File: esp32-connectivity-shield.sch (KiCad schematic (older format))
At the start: 23 parts, among them J1 DB9, P1 POWER, P2 Analog, P3 Digital, P4 Digital, P5 CONN_01X01, P6 CONN_01X01, P7 CONN_01X01, P8 CONN_01X01, U1 MCP2515-I/ST, U2 MCP2551-I/SN, Y1 16MHz

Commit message: update schematic-ethernet
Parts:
- removed C?: 0.1uF, symbol C
- removed J1: DB9, symbol DB9
- removed U1: MCP2515-I/ST, Housings_SSOP:TSSOP-20_4.4x6.5mm_Pitch0.65mm, symbol MCP2515-I/ST
- removed Y1: 16MHz, symbol Crystal
- added C10, C11, C13, C14, C15, C16, C7: 100nF, symbol C
- added C12, C8: 10u/6v3, symbol C
- added C9: 10uF/6v3, symbol C
- added J?: RJ45_LEDS, symbol RJ45_LEDS
- added L1: Ferrite_Bead CB2012D601ST, symbol Ferrite_Bead
- added L2: Ferrite_Bead, symbol Ferrite_Bead
- added P9: CONN_01X04, symbol CONN_01X04
- added R10, R13, R14, R5, R6, R7, R8, R9: 4K7, symbol R
- added R11: OR, symbol R
- added R12: 10K, symbol R
- added R15: 6k4, symbol R
- added R16, R17, R18: 330R, symbol R
- added R19: 2K2, symbol R
- added R20, R21, R22, R23: 47R, symbol R
- added U1: KS8721BL, symbol KS8721BL
- added Y1: 50MHz Crystal C7050, symbol Crystal_GND24_Small
- C1: value 22pF -> 100nF
- C2: value 22pF -> 10nF
- C3: value 0.1uF -> 100nF
- R1: value 4.7K -> 4K7
- R2: value 4.7k -> 4K7
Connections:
- net labels added: ETHERNET, ETH_RST, GPIO32, GPIO33, HEADER, LAN+2V5, LAN_RX+, LAN_RX-, LAN_TX+, LAN_TX-, LED100/DUP, LEDACT, RMII_CRS_DV, RMII_MDC, RMII_MDINT, RMII_MDIO, RMII_REF_CLK, RMII_RXD0, RMII_RXD1, RMII_TXD0, RMII_TX_EN
- net labels removed: CSO, INTO, MISO, MOSI, SCK
- wire segments 78 -> 266
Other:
- moved on the sheet: C4, C5, R3, R4, U2

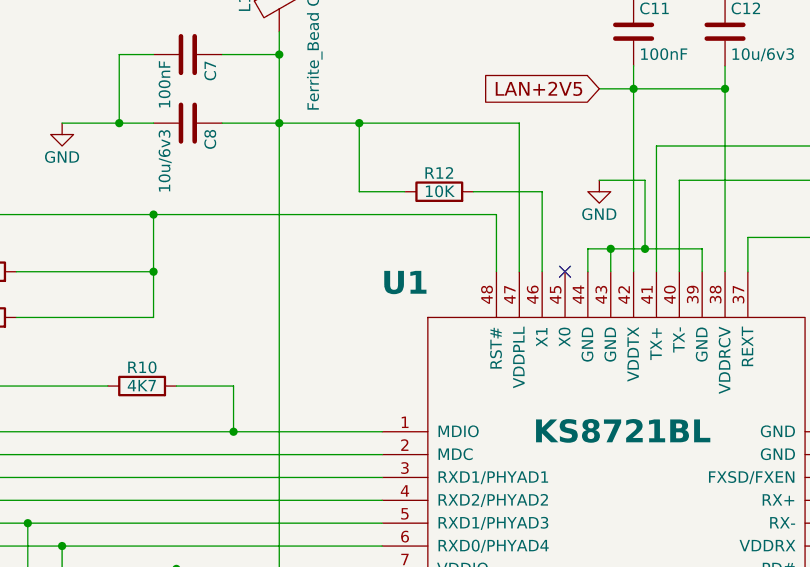
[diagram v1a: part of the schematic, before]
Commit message: fix libray error
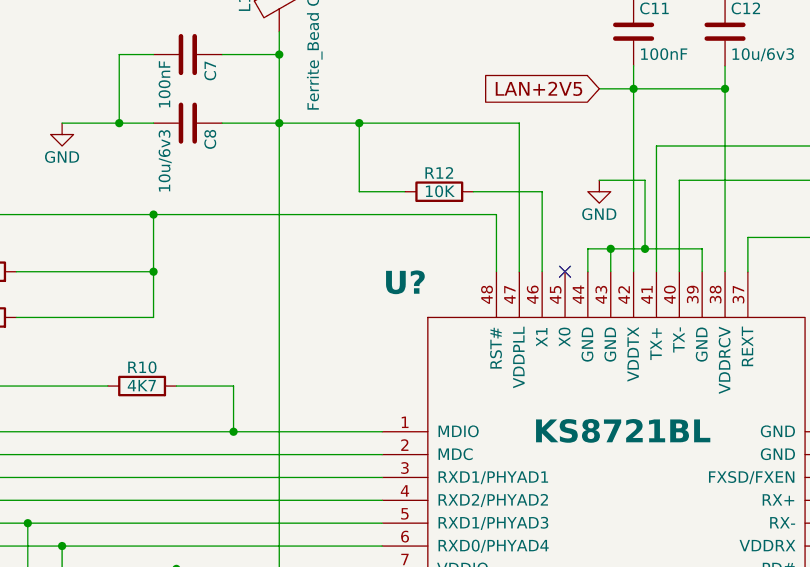
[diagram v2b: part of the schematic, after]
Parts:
- removed U1: KS8721BL, symbol KS8721BL
- added U?: KS8721BL, symbol KS8721BL
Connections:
- net 3V3: now also U?.24 (VDDIO), U?.7 (VDDIO)
- net GND: now also U?.12 (GND), U?.14 (TXER), U?.19 (TXD2), U?.20 (TXD3), U?.23 (GND), U?.35 (GND), U?.36 (GND), U?.39 (GND), U?.43 (GND), U?.44 (GND), U?.8 (GND)
- net LAN+2V5: now also U?.31 (VDDRX), U?.38 (VDDRCV), U?.42 (VDDTX)
- net LAN_RX+: now also U?.33 (RX+)
- net LAN_RX-: now also U?.32 (RX-)
- net LAN_TX+: now also U?.41 (TX+)
- net LAN_TX-: now also U?.40 (TX-)
- net RMII_CRS_DV: now also U?.9 (RXDV/PCS_LPBK)
- net RMII_MDC: now also U?.2 (MDC)
- net RMII_MDIO: now also U?.1 (MDIO)
- net RMII_REF_CLK: now also U?.15 (TXC/REF_CLK)
- net RMII_RXD0: now also U?.6 (RXD0/PHYAD4)
- net RMII_RXD1: now also U?.18 (TXD1), U?.5 (RXD1/PHYAD3)
- net RMII_TXD0: now also U?.17 (TXD0)
- net RMII_TX_EN: now also U?.16 (TXEN)
- net at C10.1, C9.1, L2.1: now also U?.13 (VDDC)
- net at R13.1: now also U?.21 (COL/RMII)
- net at R14.1: now also U?.22 (CRS/RMII_BTB)
- net at R18.2: now also U?.25 (INT#PHYAD0)
- net at R17.2: now also U?.26 (LED0/TEST)
- net at R16.2: now also U?.27 (LED1/SPD100)
- net at R1.1: now also U?.3 (RXD1/PHYAD1)
- net at R15.1: now also U?.37 (REXT)
- net at R6.1: now also U?.4 (RXD2/PHYAD2)
- net at R12.2: now also U?.46 (X1)
- net at C7.1, C8.1, L1.1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: now also U?.47 (VDDPLL)
- net at C1.1, R2.2, R5.2: now also U?.48 (RST#)
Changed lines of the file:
@@
 GPIO33
-$Comp
-L KS8721BL U1
-U 1 1 58756829
-P 5350 5600
-F 0 "U1" H 4300 6800 100 0000 C CNB
-F 1 "KS8721BL" H 5250 6150 100 0000 C CNB
-F 2 "" H 5300 4800 60  0001 C CNN
-F 3 "" H 5300 4800 60  0001 C CNN
-	1    5350 5600
-	1    0    0    -1
-$EndComp
 $Comp
 L R R10
@@
 Text Label 13450 850  0    197  ~ 39
 HEADER
+$Comp
+L KS8721BL U?
+U 1 1 58761BC4
+P 5350 5600
+F 0 "U?" H 4300 6800 100 0000 C CNB
+F 1 "KS8721BL" H 5250 6150 100 0000 C CNB
+F 2 "" H 5300 4800 60  0001 C CNN
+F 3 "" H 5300 4800 60  0001 C CNN
+	1    5350 5600
+	1    0    0    -1
+$EndComp
 $EndSCHEMATC

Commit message: add Rs232 schematic add Rs485 schematic update ethernet schematic
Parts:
- added C17: 1OOn/50V, symbol C
- added C18, C19, C20, C21, C22: 1uF, symbol C
- added J2: DB9, symbol DB9
- added P10: CONN_01X04, symbol CONN_01X04
- added P11: CONN_02X04, symbol CONN_02X04
- added R24, R25, R26: 10K, symbol R
- added U1: MAX485, symbol MAX485
- added U4: LBSS123LTIG, symbol MOSFET-P
- added U5: MAX232, symbol MAX232
- gave numbers to parts that had none: 2
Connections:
- net RMII_CRS_DV is gone; now on net IO27: R9.1, U3.9 (RXDV/PCS_LPBK)
- net RMII_MDIO is gone; now on net MATRIX: R10.2, U3.1 (MDIO)
- net RMII_REF_CLK is gone; now on net IO0: R11.1, U3.15 (TXC/REF_CLK)
- net RMII_RXD0 is gone; now on net IO25: R8.1, U3.6 (RXD0/PHYAD4)
- net RMII_TXD0 is gone; now on net IO19: U3.17 (TXD0)
- net RMII_TX_EN is gone; now on net IO21: U3.16 (TXEN)
- net 3V3: no longer C2.1
- net 5V: now also C17.1, C19.1, P10.1 (P1), R24.2, R25.2, R26.2, U1.8 (VCC), U5.16 (VCC), U5.8 (R2IN)
- net GND: now also Y1.2, C17.2, C19.2, C20.1, C22.2, J2.5, P10.4 (P4), U1.5 (GND), U4.2, U5.10 (T2IN), U5.15 (GND)
- net IO22: now also U3.18 (TXD1)
- net IO26: now also R7.1, U3.5 (RXD1/PHYAD3)
- net at Y1.4: now also C2.1
- net RMII_MDC renamed MATRIX
- net RMII_MDINT: no longer names the net of R18.1, R19.2
- removed net RMII_RXD1: R7.1, U3.18 (TXD1), U3.5 (RXD1/PHYAD3)
- net UORX renamed U0RXD
- net U0RXD: now also P11.3 (P3), P11.7 (P7)
- net UOTX renamed U0TXD
- net U0TXD: now also P11.1 (P1), P11.5 (P5)
- new net: C18.1, U5.1 (C1+)
- new net: C20.2, U5.2 (VS+)
- new net: C18.2, U5.3 (C1-)
- new net: C21.1, U5.4 (C2+)
- new net: C21.2, U5.5 (C2-)
- new net: C22.1, U5.6 (VS-)
- new net DIR_AUTO_485: R25.1, U1.2 (RE), U1.3 (DE), U4.3
- new net RS232_RX: J2.3, U5.13 (R1IN)
- new net RS232_TX: J2.2, U5.14 (T1OUT)
- new net RS485A: P10.2 (P2), U1.6 (A)
- new net RS485B: P10.3 (P3), U1.7 (B)
- new net UART_RX_232: P11.4 (P4), U5.12 (R1OUT)
- new net UART_RX_485: P11.8 (P8), U1.1 (RO)
- new net UART_TX_232: P11.2 (P2), R26.1, U5.11 (T1IN)
- new net UART_TX_485: P11.6 (P6), R24.1, U1.4 (DI), U4.1
- no-connect marks 17 -> 25
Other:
- moved on the sheet: C1, C10, C11, C12, C13, C14, C15, C16, C2, C3, C4, C5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
